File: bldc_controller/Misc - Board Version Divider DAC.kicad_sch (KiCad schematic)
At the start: 2 parts

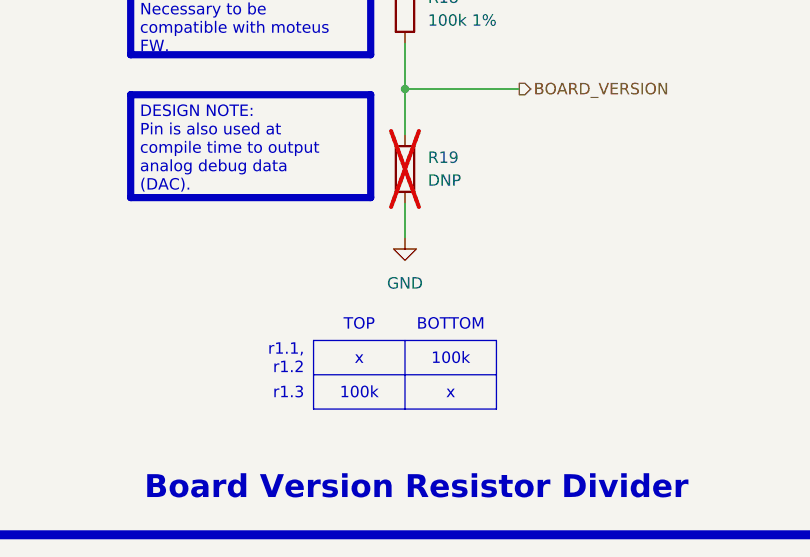
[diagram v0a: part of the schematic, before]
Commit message: schematic is complete. Replaced 5V buck and added pi filters.
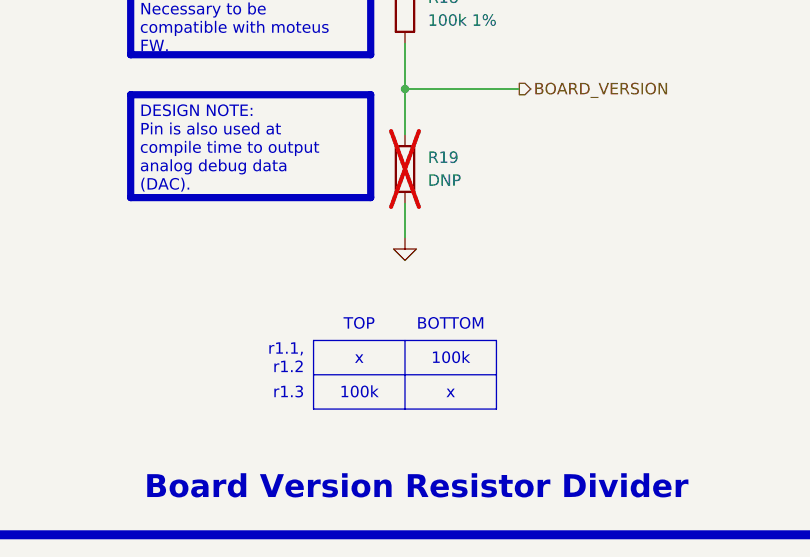
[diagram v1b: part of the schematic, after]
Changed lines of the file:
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@@
-    )
-  )
-  (symbol (lib_id "power:GND") (at 149.86 100.33 0) (unit 1)
-    (in_bom yes) (on_board yes) (dnp no) (fields_autoplaced)
-    (property "Reference" "#PWR038" (at 149.86 106.68 0)
-      (effects (font (size 1.27 1.27)) hide)
-    )
-    (property "Value" "GND" (at 149.86 105.41 0)
-      (effects (font (size 1.27 1.27)))
-    )
-    (property "Footprint" "" (at 149.86 100.33 0)
-      (effects (font (size 1.27 1.27)) hide)
-    )
-    (property "Datasheet" "" (at 149.86 100.33 0)
-      (effects (font (size 1.27 1.27)) hide)
-    )
-    (pin "1")
-    (instances
-      (project "bldc_controller"
-        (path "/0650c7a8-acba-429c-9f8e-eec0baf0bc1c/fede4c36-00cc-4d3d-b71c-5243ba232202/07dcaf51-abc9-470d-8bd8-30b1c54b6fbd"
-          (reference "#PWR038") (unit 1)
-        )
-      )
     )
   )
@@
         )
       )
+    )
+  )
+  (symbol (lib_id "power:GND") (at 149.86 100.33 0) (unit 1)
+    (in_bom yes) (on_board yes) (dnp no) (fields_autoplaced)
+    (property "Reference" "#PWR032" (at 149.86 106.68 0)
+      (effects (font (size 1.27 1.27)) hide)
+    )
+    (property "Value" "GND" (at 149.86 105.41 0)
+      (effects (font (size 1.27 1.27)) hide)
+    )
+    (property "Footprint" "" (at 149.86 100.33 0)
+      (effects (font (size 1.27 1.27)) hide)
+    )
+    (property "Datasheet" "" (at 149.86 100.33 0)
+      (effects (font (size 1.27 1.27)) hide)
+    )
+    (pin "1")
+    (instances
+      (project "bldc_controller"
+        (path "/0650c7a8-acba-429c-9f8e-eec0baf0bc1c/fede4c36-00cc-4d3d-b71c-5243ba232202/07dcaf51-abc9-470d-8bd8-30b1c54b6fbd"
+          (reference "#PWR032") (unit 1)
+        )
+      )

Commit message: added assembly files
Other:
- moved on the sheet: R18, R19
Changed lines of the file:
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@@
     (company "${COMPANY}")
   )
-  (junction (at 149.86 83.82) (diameter 0) (color 0 0 0 0)
+  (junction (at 149.86 78.74) (diameter 0) (color 0 0 0 0)
   )
-  (wire (pts (xy 149.86 83.82) (xy 149.86 78.74))
+  (wire (pts (xy 149.86 78.74) (xy 149.86 73.66))
     (stroke (width 0) (type default))
   )
-  (polyline (pts (xy 149.86 111.76) (xy 149.86 119.38))
+  (wire (pts (xy 149.86 78.74) (xy 149.86 83.82))
     (stroke (width 0) (type default))
   )
-  (wire (pts (xy 149.86 83.82) (xy 149.86 88.9))
+  (wire (pts (xy 162.56 78.74) (xy 149.86 78.74))
     (stroke (width 0) (type default))
   )
-  (wire (pts (xy 162.56 83.82) (xy 149.86 83.82))
+  (wire (pts (xy 149.86 59.69) (xy 149.86 66.04))
     (stroke (width 0) (type default))
   )
-  (wire (pts (xy 149.86 64.77) (xy 149.86 71.12))
+  (wire (pts (xy 149.86 95.25) (xy 149.86 91.44))
     (stroke (width 0) (type default))
   )
-  (polyline (pts (xy 139.7 115.57) (xy 160.02 115.57))
-    (stroke (width 0) (type default))
+  (rectangle (start 139.7 111.252) (end 177.8 112.014)
+    (stroke (width 0) (type default) (color 0 0 0 1))
+    (fill (type color) (color 0 0 0 1))
   )
-  (wire (pts (xy 149.86 100.33) (xy 149.86 96.52))
-    (stroke (width 0) (type default))
-  )
-  (rectangle (start 104.14 49.53) (end 198.12 133.35)
+  (rectangle (start 104.14 44.45) (end 198.12 140.97)
     (stroke (width 1) (type default) (color 200 200 200 1))
     (fill (type none))
   )
-  (rectangle (start 139.7 111.76) (end 160.02 119.38)
-    (stroke (width 0) (type default))
+  (rectangle (start 137.922 113.03) (end 138.684 128.27)
+    (stroke (width 0) (type default) (color 0 0 0 1))
+    (fill (type color) (color 0 0 0 1))
+  )
+  (text_box "×"
+    (at 158.75 120.65 0) (size 19.05 7.62)
+    (stroke (width 0) (type default) (color 0 0 0 1))
     (fill (type none))
+    (effects (font (face "Times New Roman") (size 4 4) bold (color 0 0 127 1)))
   )
-  (text_box "100k"
-    (at 149.86 111.76 0) (size 10.16 3.81)
-    (stroke (width -0.0001) (type default))
+  (text_box "r1.3"
+    (at 121.92 120.65 0) (size 16.51 7.62)
+    (stroke (width 0) (type default) (color 0 0 0 1))
     (fill (type none))
-    (effects (font (face "Arial") (size 1.27 1.27) (color 0 0 0 1)))
+    (effects (font (face "Times New Roman") (size 2.286 2.286) bold (color 0 0 127 1)))
+  )
+  (text_box "r1.1, r1.2"
+    (at 121.92 113.03 0) (size 16.51 7.62)
+    (stroke (width 0) (type default) (color 0 0 0 1))
+    (fill (type none))
+    (effects (font (face "Times New Roman") (size 2.286 2.286) bold (color 0 0 127 1)))
   )
   (text_box "DESIGN NOTE:\nNecessary to be compatible with moteus FW."
-    (at 119.38 71.12 0) (size 26.67 8.89)
+    (at 119.38 66.04 0) (size 26.67 8.89)
     (stroke (width 0.8) (type solid) (color 255 165 0 1))
     (fill (type none))
     (effects (font (face "Arial") (size 1.27 1.27) (color 0 0 0 1)) (justify left top))
   )
-  (text_box "BOTTOM"
-    (at 149.86 107.95 0) (size 10.16 3.81)
-    (stroke (width -0.0001) (type default))
+  (text_box "100k"
+    (at 139.7 120.65 0) (size 19.05 7.62)
+    (stroke (width 0) (type default) (color 0 0 0 1))
     (fill (type none))
-    (effects (font (face "Arial") (size 1.27 1.27) (color 0 0 0 1)))
-  )
-  (text_box "x"
-    (at 139.7 111.76 0) (size 10.16 3.81)
-    (stroke (width -0.0001) (type default))
-    (fill (type none))
-    (effects (font (face "Arial") (size 1.27 1.27) (color 0 0 0 1)))
+    (effects (font (face "Times New Roman") (size 2.286 2.286) bold (color 0 0 127 1)))
   )
   (text_box "[${#}] ${TITLE}"
@@
     (effects (font (face "Times New Roman") (size 6 6) (thickness 1.2) bold (color 162 22 34 1)))
   )
-  (text_box "r1.3"
-    (at 129.54 115.57 0) (size 10.16 3.81)
-    (stroke (width -0.0001) (type default))
-    (fill (type none))
-    (effects (font (face "Arial") (size 1.27 1.27) (color 0 0 0 1)) (justify right))
-  )
   (text_box "DESIGN NOTE:\nPin is also used at compile time to output analog debug data (DAC)."
-    (at 119.38 84.455 0) (size 26.67 11.43)
+    (at 119.38 79.375 0) (size 26.67 11.43)
     (stroke (width 0.8) (type solid) (color 200 200 200 1))
     (fill (type none))
@@
   )
   (text_box "100k"
-    (at 139.7 115.57 0) (size 10.16 3.81)
-    (stroke (width -0.0001) (type default))
+    (at 158.75 113.03 0) (size 19.05 7.62)
+    (stroke (width 0) (type default) (color 0 0 0 1))
     (fill (type none))
-    (effects (font (face "Arial") (size 1.27 1.27) (color 0 0 0 1)))
-  )
-  (text_box "TOP"
-    (at 139.7 107.95 0) (size 10.16 3.81)
-    (stroke (width -0.0001) (type default))
-    (fill (type none))
-    (effects (font (face "Arial") (size 1.27 1.27) (color 0 0 0 1)))
-  )
-  (text_box "x"
-    (at 149.86 115.57 0) (size 10.16 3.81)
-    (stroke (width -0.0001) (type default))
-    (fill (type none))
-    (effects (font (face "Arial") (size 1.27 1.27) (color 0 0 0 1)))
+    (effects (font (face "Times New Roman") (size 2.286 2.286) bold (color 0 0 127 1)))
   )
   (text_box "Board Version Resistor Divider"
-    (at 105.41 121.92 0) (size 91.44 9.525)
+    (at 105.41 129.54 0) (size 91.44 9.525)
     (stroke (width -0.0001) (type default))
     (fill (type none))
     (effects (font (face "Times New Roman") (size 2.54 2.54) (thickness 0.508) bold (color 162 22 34 1)) (justify bottom))
   )
-  (text_box "r1.1, r1.2"
-    (at 129.54 111.76 0) (size 10.16 3.81)
-    (stroke (width -0.0001) (type default))
+  (text_box "BOTTOM"
+    (at 158.75 104.14 0) (size 19.05 7.62)
+    (stroke (width 0) (type default) (color 0 0 0 1))
     (fill (type none))
-    (effects (font (face "Arial") (size 1.27 1.27) (color 0 0 0 1)) (justify right))
+    (effects (font (face "Times New Roman") (size 2.286 2.286) bold (color 0 0 127 1)))
   )
-  (hierarchical_label "BOARD_VERSION" (shape output) (at 162.56 83.82 0) (fields_autoplaced)
+  (text_box "×"
+    (at 139.7 113.03 0) (size 19.05 7.62)
+    (stroke (width 0) (type default) (color 0 0 0 1))
+    (fill (type none))
+    (effects (font (face "Times New Roman") (size 4 4) bold (color 0 0 127 1)))
+  )
+  (text_box "TOP"
+    (at 139.7 104.14 0) (size 19.05 7.62)
+    (stroke (width 0) (type default) (color 0 0 0 1))
+    (fill (type none))
+    (effects (font (face "Times New Roman") (size 2.286 2.286) bold (color 0 0 127 1)))
+  )
+  (hierarchical_label "BOARD_VERSION" (shape output) (at 162.56 78.74 0) (fields_autoplaced)
     (effects (font (face "Arial") (size 1.27 1.27)) (justify left))
   )
-  (symbol (lib_id "Device:R") (at 149.86 92.71 0) (unit 1)
+  (symbol (lib_id "Device:R") (at 149.86 87.63 0) (unit 1)
     (in_bom no) (on_board yes) (dnp yes) (fields_autoplaced)
-    (property "Reference" "R19" (at 152.4 91.44 0)
+    (property "Reference" "R19" (at 152.4 86.36 0)
       (effects (font (size 1.27 1.27)) (justify left))
     )
-    (property "Value" "DNP" (at 152.4 93.98 0)
+    (property "Value" "DNP" (at 152.4 88.9 0)
       (effects (font (size 1.27 1.27)) (justify left))
     )
-    (property "Footprint" "0_resistor_smd:R_0402_1005_DensityHigh" (at 148.082 92.71 90)
+    (property "Footprint" "0_resistor_smd:R_0402_1005_DensityHigh" (at 148.082 87.63 90)
       (effects (font (size 1.27 1.27)) hide)
     )
-    (property "Datasheet" "~" (at 149.86 92.71 0)
+    (property "Datasheet" "~" (at 149.86 87.63 0)
       (effects (font (size 1.27 1.27)) hide)
     )
@@
     )
   )
-  (symbol (lib_id "power:+3V3") (at 149.86 64.77 0) (unit 1)
+  (symbol (lib_id "power:+3V3") (at 149.86 59.69 0) (unit 1)
     (in_bom yes) (on_board yes) (dnp no) (fields_autoplaced)
-    (property "Reference" "#PWR037" (at 149.86 68.58 0)
+    (property "Reference" "#PWR037" (at 149.86 63.5 0)
       (effects (font (size 1.27 1.27)) hide)
     )
-    (property "Value" "+3V3" (at 149.86 59.69 0)
+    (property "Value" "+3V3" (at 149.86 54.61 0)
       (effects (font (size 1.27 1.27)))
     )
-    (property "Footprint" "" (at 149.86 64.77 0)
+    (property "Footprint" "" (at 149.86 59.69 0)
       (effects (font (size 1.27 1.27)) hide)
     )
-    (property "Datasheet" "" (at 149.86 64.77 0)
+    (property "Datasheet" "" (at 149.86 59.69 0)
       (effects (font (size 1.27 1.27)) hide)
     )
@@
     )
   )
-  (symbol (lib_id "Device:R") (at 149.86 74.93 0) (unit 1)
+  (symbol (lib_id "Device:R") (at 149.86 69.85 0) (unit 1)
     (in_bom yes) (on_board yes) (dnp no) (fields_autoplaced)
-    (property "Reference" "R18" (at 152.4 73.66 0)
+    (property "Reference" "R18" (at 152.4 68.58 0)
       (effects (font (size 1.27 1.27)) (justify left))
     )
-    (property "Value" "100k 1%" (at 152.4 76.2 0)
+    (property "Value" "100k 1%" (at 152.4 71.12 0)
       (effects (font (size 1.27 1.27)) (justify left))
     )
-    (property "Footprint" "0_resistor_smd:R_0402_1005_DensityHigh" (at 148.082 74.93 90)
+    (property "Footprint" "0_resistor_smd:R_0402_1005_DensityHigh" (at 148.082 69.85 90)
       (effects (font (size 1.27 1.27)) hide)
     )
-    (property "Datasheet" "~" (at 149.86 74.93 0)
+    (property "Datasheet" "~" (at 149.86 69.85 0)
       (effects (font (size 1.27 1.27)) hide)
     )
@@
     )
   )
-  (symbol (lib_id "power:GND") (at 149.86 100.33 0) (unit 1)
+  (symbol (lib_id "power:GND") (at 149.86 95.25 0) (unit 1)
     (in_bom yes) (on_board yes) (dnp no) (fields_autoplaced)
-    (property "Reference" "#PWR032" (at 149.86 106.68 0)
+    (property "Reference" "#PWR032" (at 149.86 101.6 0)
       (effects (font (size 1.27 1.27)) hide)
     )
-    (property "Value" "GND" (at 149.86 105.41 0)
+    (property "Value" "GND" (at 149.86 100.33 0)
       (effects (font (size 1.27 1.27)) hide)
     )
-    (property "Footprint" "" (at 149.86 100.33 0)
+    (property "Footprint" "" (at 149.86 95.25 0)
       (effects (font (size 1.27 1.27)) hide)
     )
-    (property "Datasheet" "" (at 149.86 100.33 0)
+    (property "Datasheet" "" (at 149.86 95.25 0)
       (effects (font (size 1.27 1.27)) hide)
     )
